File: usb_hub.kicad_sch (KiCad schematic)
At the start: 89 parts, among them J5 USB-C_WE_632723300011, J6 USB-C_WE_632723300011, U16 AP7366_SOT, U17 TPD4E05U06QDQARQ1, U18 AP22615A_TSOT26, U19 TPD4E05U06QDQARQ1, U20 AP22615A_TSOT26, U21 USB7252C, U22 W25Q80DV_USON, U24 TPD4E05U06QDQARQ1, U25 TPD4E05U06QDQARQ1, U27 TPD4E05U06QDQARQ1, U28 TPD4E05U06QDQARQ1, Y2 Oscillator_25MHz_ESC_2016MV

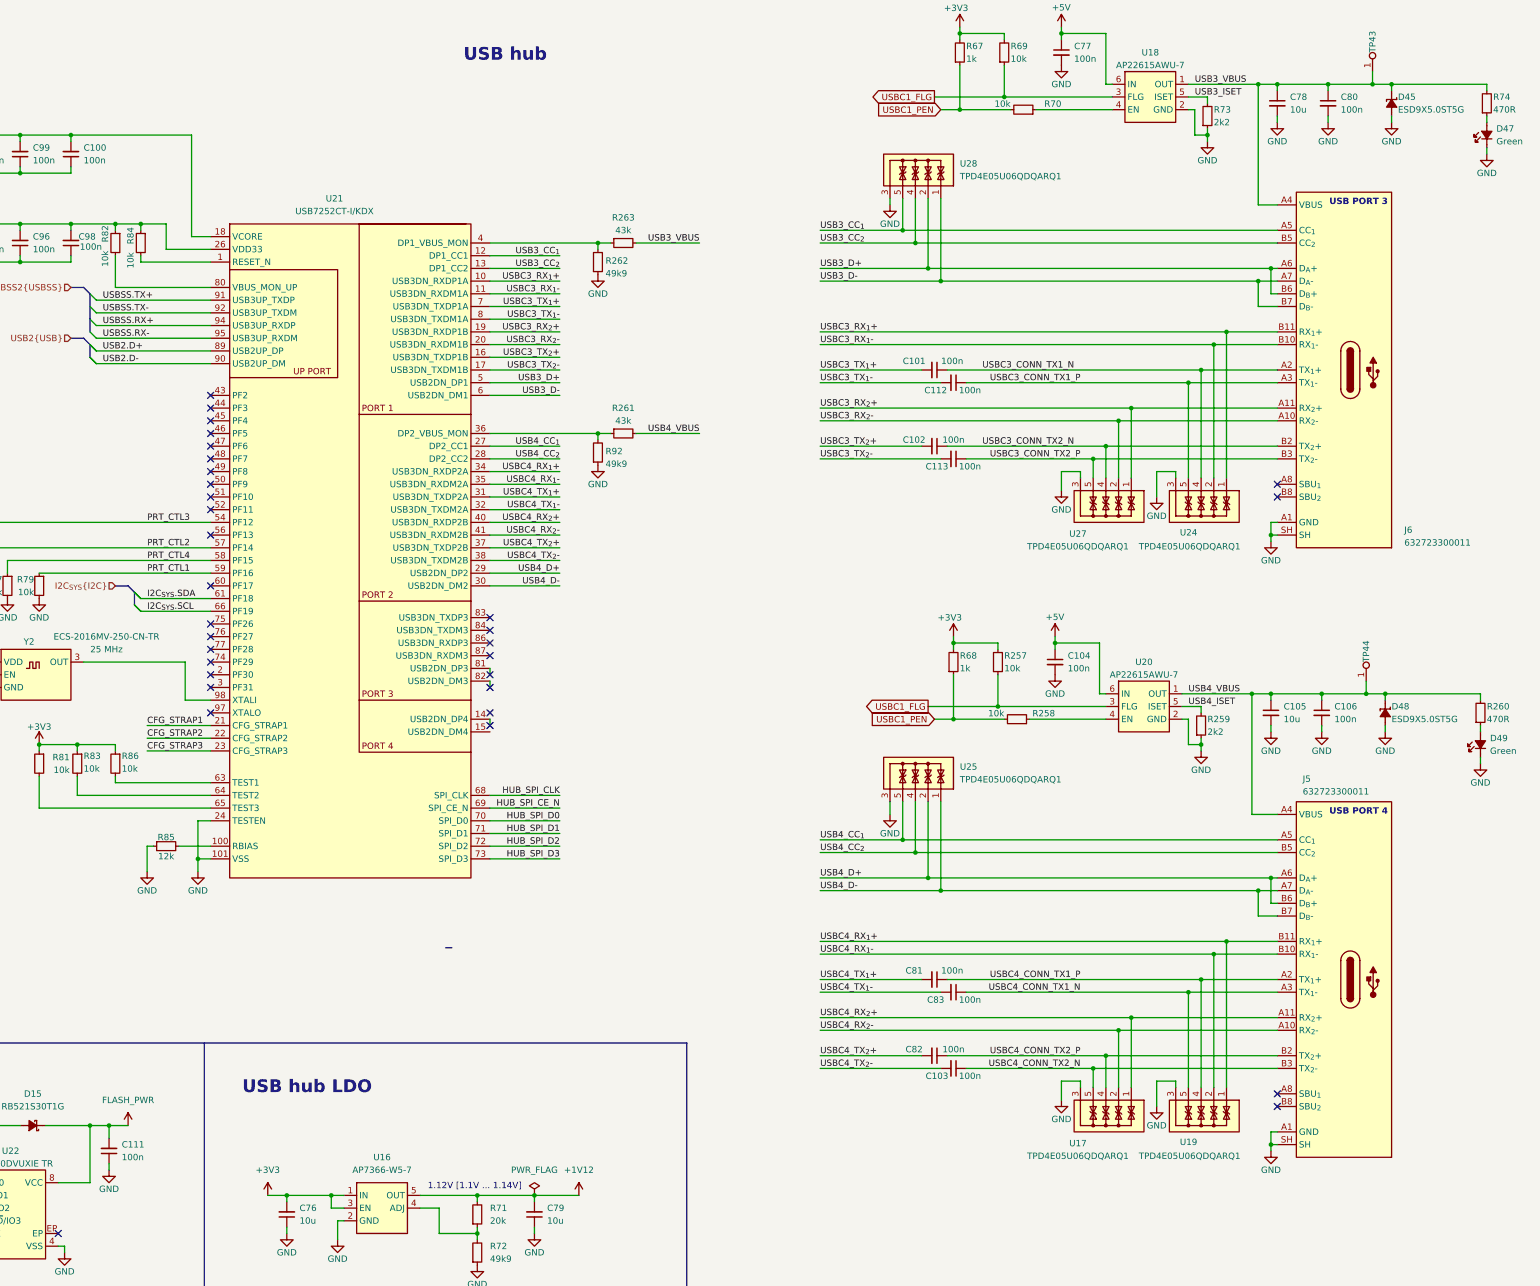
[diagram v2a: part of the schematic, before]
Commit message: [#82837] Finish USB Hub sheet
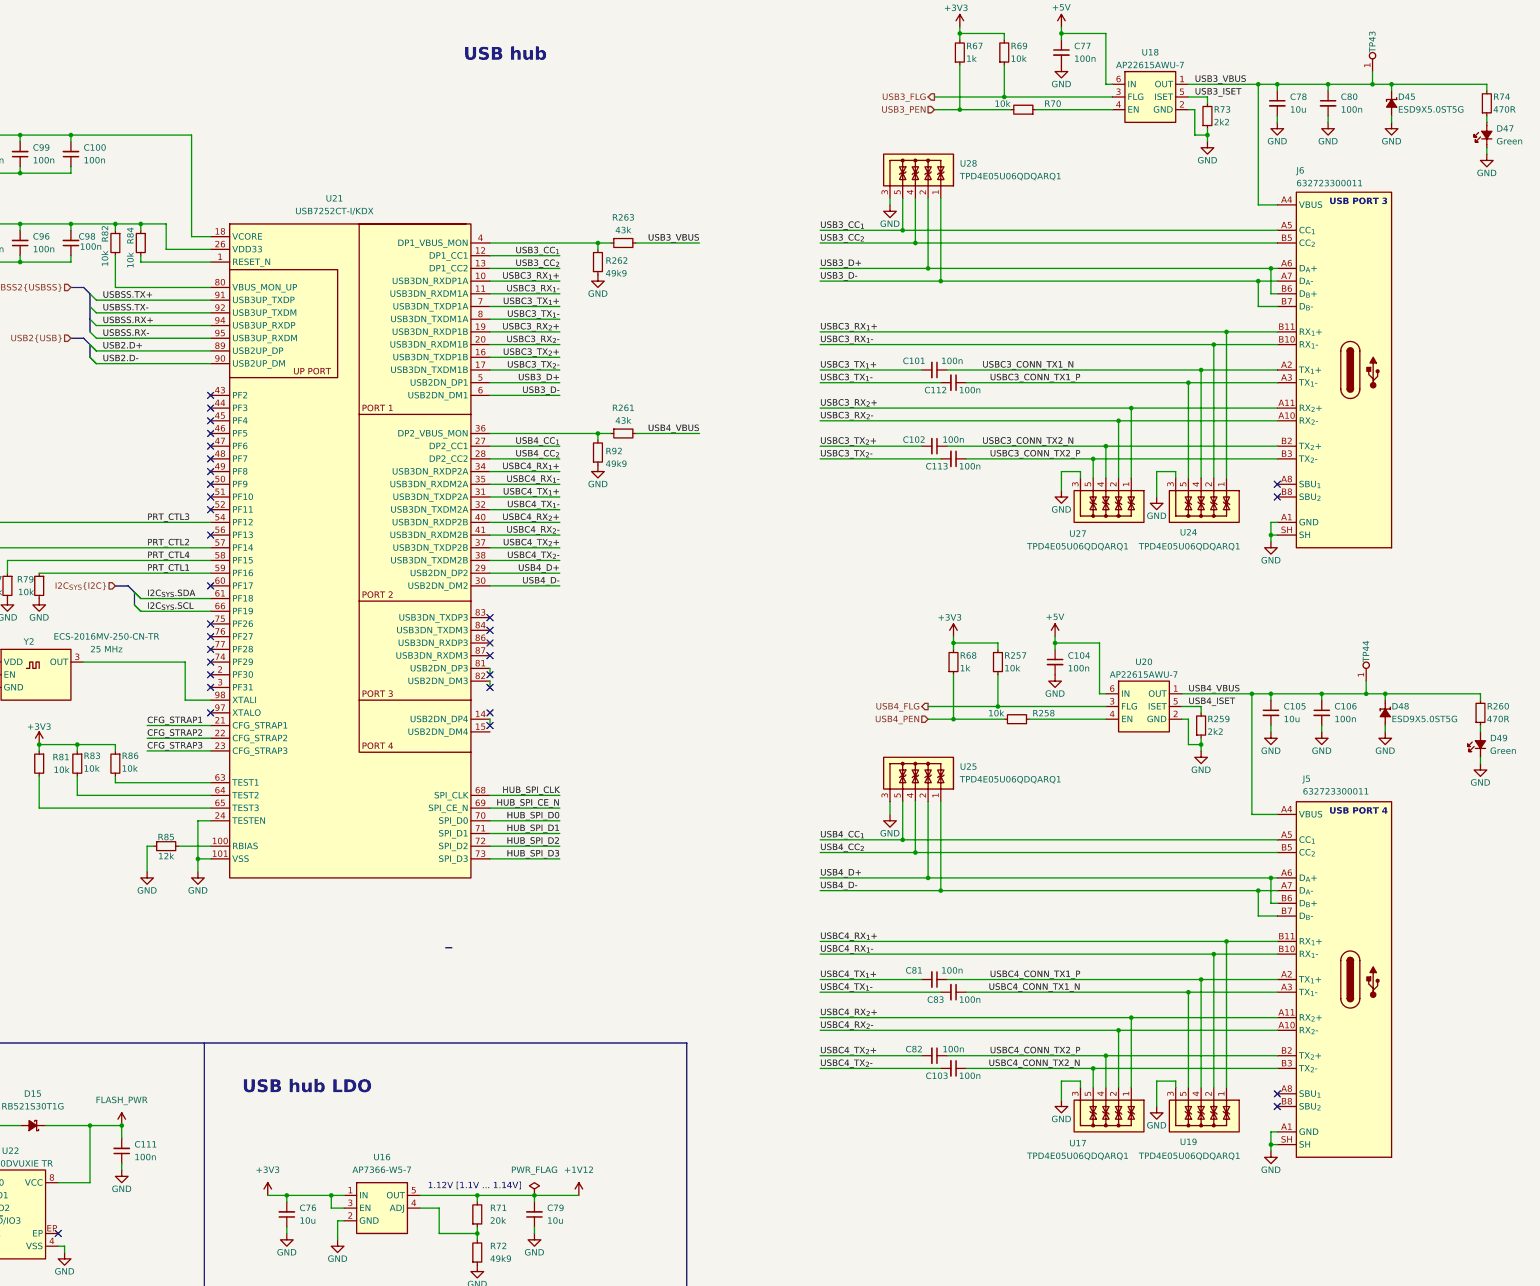
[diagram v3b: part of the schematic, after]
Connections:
- net USBC1_FLG renamed USB3_FLG
- net USB3_FLG: no longer R257.1, U20.3 (FLG)
- net USBC1_PEN renamed USB3_PEN
- net USB3_PEN: no longer R258.2, R68.1
- new net USB4_FLG: R257.1, U20.3 (FLG)
- new net USB4_PEN: R258.2, R68.1
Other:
- moved on the sheet: C111
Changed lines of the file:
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@@
 	)
 	(junction
-		(at 118.11 240.03)
-		(diameter 0)
-		(color 0 0 0 0)
-	)
-	(junction
 		(at 276.86 182.88)
 		(diameter 0)
@@
 	)
 	(junction
+		(at 120.65 240.03)
+		(diameter 0)
+		(color 0 0 0 0)
+	)
+	(junction
 		(at 114.3 240.03)
 		(diameter 0)
@@
 	(wire
 		(pts
-			(xy 118.11 247.65) (xy 118.11 248.92)
+			(xy 120.65 247.65) (xy 120.65 248.92)
 		)
 		(stroke
@@
 	(wire
 		(pts
-			(xy 118.11 240.03) (xy 118.11 242.57)
+			(xy 120.65 240.03) (xy 120.65 242.57)
 		)
 		(stroke
@@
 	(wire
 		(pts
-			(xy 114.3 240.03) (xy 118.11 240.03)
+			(xy 114.3 240.03) (xy 120.65 240.03)
 		)
 		(stroke
@@
 	(wire
 		(pts
+			(xy 283.21 36.83) (xy 288.29 36.83)
+		)
+		(stroke
+			(width 0)
+			(type default)
+		)
+	)
+	(wire
+		(pts
 			(xy 322.58 96.52) (xy 322.58 110.49)
 		)
@@
 	(wire
 		(pts
+			(xy 281.94 158.75) (xy 287.02 158.75)
+		)
+		(stroke
+			(width 0)
+			(type default)
+		)
+	)
+	(wire
+		(pts
 			(xy 54.61 276.86) (xy 81.28 276.86)
 		)
@@
 	(wire
 		(pts
-			(xy 283.21 158.75) (xy 287.02 158.75)
-		)
-		(stroke
-			(width 0)
-			(type default)
-		)
-	)
-	(wire
-		(pts
 			(xy 125.73 165.1) (xy 138.43 165.1)
 		)
@@
 	(wire
 		(pts
-			(xy 118.11 240.03) (xy 121.92 240.03)
-		)
-		(stroke
-			(width 0)
-			(type default)
-		)
-	)
-	(wire
-		(pts
 			(xy 276.86 175.26) (xy 276.86 182.88)
 		)
@@
 	(wire
 		(pts
-			(xy 284.48 36.83) (xy 288.29 36.83)
-		)
-		(stroke
-			(width 0)
-			(type default)
-		)
-	)
-	(wire
-		(pts
 			(xy 80.01 41.91) (xy 90.17 41.91)
 		)
@@
 		)
 	)
-	(global_label "USBC1_PEN"
+	(hierarchical_label "SPI_{HUB_DEBUG}{SPI}"
 		(shape input)
-		(at 283.21 158.75 180)
+		(at 49.53 269.24 180)
 		(effects
 			(font
@@
 			(justify right)
 		)
-		(property "Intersheetrefs" "${INTERSHEET_REFS}"
-			(at 269.24 158.75 0)
-			(effects
-				(font
-					(size 1.27 1.27)
-				)
-				(justify right)
-				(hide yes)
-			)
-		)
 	)
-	(global_label "USBC1_FLG"
-		(shape output)
-		(at 283.21 34.29 180)
+	(hierarchical_label "USB2{USB}"
+		(shape input)
+		(at 110.49 82.55 180)
 		(effects
 			(font
@@
 			(justify right)
 		)
-		(property "Intersheetrefs" "${INTERSHEET_REFS}"
-			(at 269.24 34.29 0)
-			(effects
-				(font
-					(size 1.27 1.27)
-				)
-				(justify right)
-				(hide yes)
-			)
-		)
 	)
-	(global_label "USBC1_PEN"
+	(hierarchical_label "USB4_PEN"
 		(shape input)
-		(at 284.48 36.83 180)
+		(at 281.94 158.75 180)
 		(effects
 			(font
@@
 			(justify right)
 		)
-		(property "Intersheetrefs" "${INTERSHEET_REFS}"
-			(at 270.51 36.83 0)
-			(effects
-				(font
-					(size 1.27 1.27)
-				)
-				(justify right)
-				(hide yes)
-			)
-		)
 	)
-	(global_label "USBC1_FLG"
+	(hierarchical_label "USB4_FLG"
 		(shape output)
 		(at 281.94 156.21 180)
@@
 			(justify right)
 		)
-		(property "Intersheetrefs" "${INTERSHEET_REFS}"
-			(at 267.97 156.21 0)
-			(effects
-				(font
-					(size 1.27 1.27)
-				)
-				(justify right)
-				(hide yes)
-			)
-		)
 	)
-	(hierarchical_label "SPI_{HUB_DEBUG}{SPI}"
+	(hierarchical_label "I2C_{SYS}{I2C}"
 		(shape input)
-		(at 49.53 269.24 180)
+		(at 119.38 132.08 180)
 		(effects
 			(font
@@
 		)
 	)
-	(hierarchical_label "USB2{USB}"
+	(hierarchical_label "USB3_PEN"
 		(shape input)
-		(at 110.49 82.55 180)
+		(at 283.21 36.83 180)
 		(effects
 			(font
@@
 		)
 	)
-	(hierarchical_label "I2C_{SYS}{I2C}"
-		(shape input)
-		(at 119.38 132.08 180)
+	(hierarchical_label "USB3_FLG"
+		(shape output)
+		(at 283.21 34.29 180)
 		(effects
 			(font
@@
 		(lib_name "GND_3")
 		(lib_id "antmicropower:GND")
-		(at 118.11 248.92 0)
+		(at 120.65 248.92 0)
 		(mirror y)
 		(unit 1)
@@
 		(dnp no)
 		(property "Reference" "#PWR0203"
-			(at 118.11 255.27 0)
+			(at 120.65 255.27 0)
 			(effects
 				(font
@@
 		)
 		(property "Value" "GND"
-			(at 118.11 252.73 0)
+			(at 120.65 252.73 0)
 			(effects
 				(font
@@
 		)
 		(property "Footprint" ""
-			(at 109.22 256.54 0)
+			(at 111.76 256.54 0)
 			(effects
 				(font
@@
 		)
 		(property "Datasheet" ""
-			(at 109.22 261.62 0)
+			(at 111.76 261.62 0)
 			(effects
 				(font
@@
 		)
 		(property "Description" ""
-			(at 118.11 248.92 0)
+			(at 120.65 248.92 0)
 			(effects
 				(font
@@
 		)
 		(property "Author" "Antmicro"
-			(at 109.22 256.54 0)
+			(at 111.76 256.54 0)
 			(effects
 				(font
@@
 		)
 		(property "License" "Apache-2.0"
-			(at 109.22 259.08 0)
+			(at 111.76 259.08 0)
 			(effects
 				(font
@@
 		(dnp no)
 		(property "Reference" "J6"
-			(at 377.19 120.904 0)
+			(at 355.6 49.022 0)
 			(effects
 				(font
@@
 		)
 		(property "MPN" "632723300011"
-			(at 377.19 123.444 0)
+			(at 355.6 51.562 0)
 			(effects
 				(font
@@
 	(symbol
 		(lib_id "antmicropower:+3V3")
-		(at 121.92 240.03 0)
+		(at 120.65 240.03 0)
 		(unit 1)
 		(exclude_from_sim no)
@@
 		(fields_autoplaced yes)
 		(property "Reference" "#PWR0204"
-			(at 137.16 240.03 0)
+			(at 135.89 240.03 0)
 			(effects
 				(font
@@
 		)
 		(property "Value" "FLASH_PWR"
-			(at 121.92 234.95 0)
+			(at 120.65 234.95 0)
 			(effects
 				(font
@@
 		)
 		(property "Footprint" ""
-			(at 137.16 247.65 0)
+			(at 135.89 247.65 0)
 			(effects
 				(font
@@
 		)
 		(property "Datasheet" ""
-			(at 137.16 250.19 0)
+			(at 135.89 250.19 0)
 			(effects
 				(font
@@
 		)
 		(property "Description" ""
-			(at 121.92 240.03 0)
+			(at 120.65 240.03 0)
 			(effects
 				(font
@@
 		)
 		(property "Author" "Antmicro"
-			(at 137.16 242.57 0)
+			(at 135.89 242.57 0)
 			(effects
 				(font
@@
 		)
 		(property "License" "Apache-2.0"
-			(at 137.16 245.11 0)
+			(at 135.89 245.11 0)
 			(effects
 				(font
@@
 		(lib_name "C_100n_0402_2")
 		(lib_id "antmicroCapacitors0402:C_100n_0402")
-		(at 118.11 247.65 90)
+		(at 120.65 247.65 90)
 		(unit 1)
 		(exclude_from_sim no)
@@
 		(fields_autoplaced yes)
 		(property "Reference" "C111"
-			(at 120.65 243.8336 90)
+			(at 123.19 243.8336 90)
 			(effects
 				(font
@@
 		)
 		(property "Value" "C_100n_0402"
-			(at 128.27 227.33 0)
+			(at 130.81 227.33 0)
 			(effects
 				(font
@@
 		)
 		(property "Footprint" "antmicro-footprints:C_0402_1005Metric"
-			(at 130.81 227.33 0)
+			(at 133.35 227.33 0)
 			(effects
 				(font
@@
 		)
 		(property "Datasheet" "https://www.murata.com/products/productdetail?partno=GRM155R61H104KE14%23"
-			(at 133.35 227.33 0)
+			(at 135.89 227.33 0)
 			(effects
 				(font
@@
 		)
 		(property "Description" ""
-			(at 118.11 247.65 0)
+			(at 120.65 247.65 0)
 			(effects
 				(font
@@
 		)
 		(property "Manufacturer" "Murata"
-			(at 138.43 227.33 0)
+			(at 140.97 227.33 0)
 			(effects
 				(font
@@
 		)
 		(property "MPN" "GRM155R61H104KE14D"
-			(at 135.89 227.33 0)
+			(at 138.43 227.33 0)
 			(effects
 				(font
@@
 		)
 		(property "Val" "100n"
-			(at 120.65 246.3736 90)
+			(at 123.19 246.3736 90)
 			(effects
 				(font
@@
 		)
 		(property "License" "Apache-2.0"
-			(at 140.97 227.33 0)
+			(at 143.51 227.33 0)
 			(effects
 				(font
@@
 		)
 		(property "Author" "Antmicro"
-			(at 143.51 227.33 0)
+			(at 146.05 227.33 0)
 			(effects
 				(font
@@
 		)
 		(property "Voltage" "50V"
-			(at 146.05 227.33 0)
+			(at 148.59 227.33 0)
 			(effects
 				(font
@@
 		)
 		(property "Dielectric" "X5R"
-			(at 148.59 227.33 0)
+			(at 151.13 227.33 0)
 			(effects
 				(font

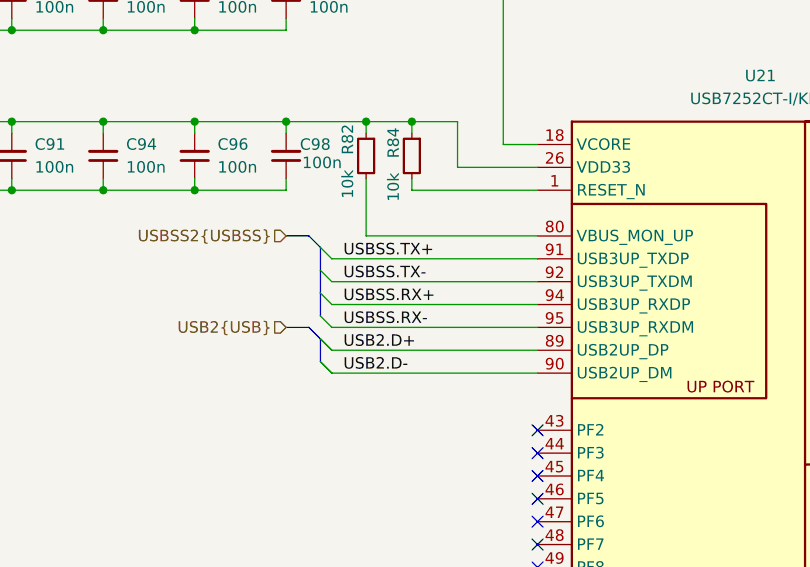
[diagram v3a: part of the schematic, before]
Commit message: [#82837] Fix USB recovery and flashing section
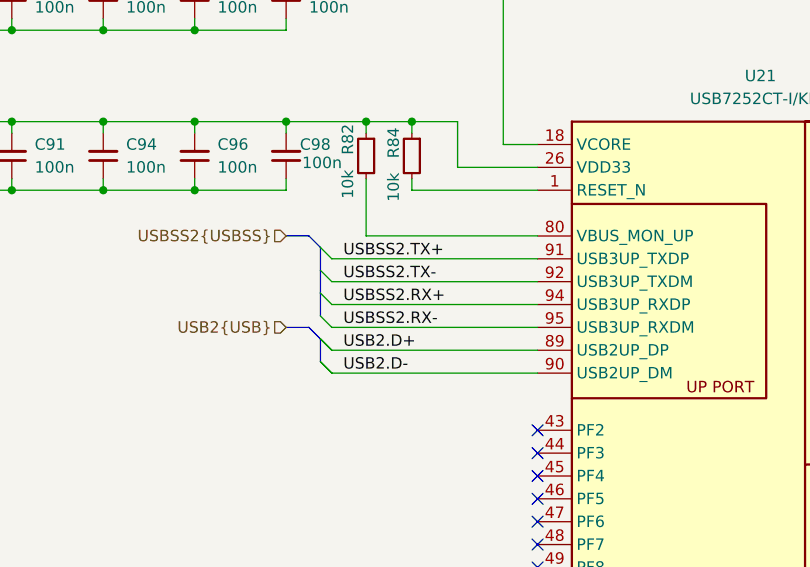
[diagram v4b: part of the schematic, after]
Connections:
- net USBSS.RX+ renamed USBSS2.RX+
- net USBSS.RX- renamed USBSS2.RX-
- net USBSS.TX+ renamed USBSS2.TX+
- net USBSS.TX- renamed USBSS2.TX-
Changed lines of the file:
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@@
 		)
 	)
-	(label "USBSS.TX+"
+	(label "USBSS2.TX+"
 		(at 116.84 74.93 0)
 		(effects
@@
 		)
 	)
-	(label "USBSS.RX+"
+	(label "USBSS2.RX+"
 		(at 116.84 80.01 0)
 		(effects
@@
 		)
 	)
-	(label "USBSS.RX-"
+	(label "USBSS2.RX-"
 		(at 116.84 82.55 0)
 		(effects
@@
 		)
 	)
-	(label "USBSS.TX-"
+	(label "USBSS2.TX-"
 		(at 116.84 77.47 0)
 		(effects
